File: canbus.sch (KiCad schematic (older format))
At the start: 15 parts, among them J1 Conn_01x08, J2 RJ45, J3 RJ45, U1 MCP2515-E/SO, U2 MCP2562-H/SN, Y1 Crystal_GND24

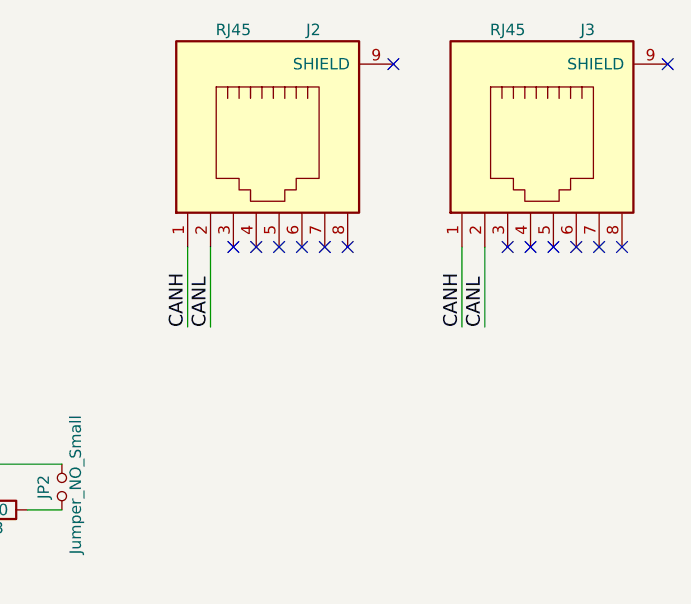
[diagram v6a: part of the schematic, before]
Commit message: Added gnd to RJ45 and connected all pins for passthrough
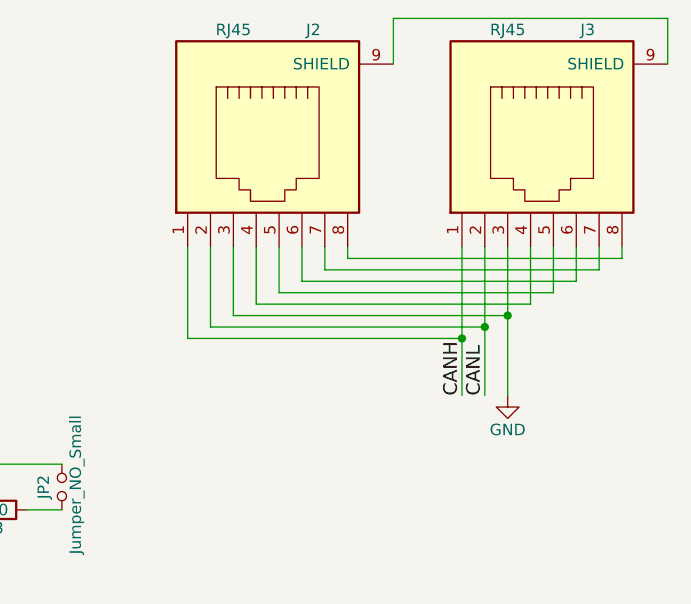
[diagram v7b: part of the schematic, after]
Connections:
- net GND: now also J2.3, J3.3
- net at J2.4: now also J3.4
- net at J2.5: now also J3.5
- net at J2.6: now also J3.6
- net at J2.7: now also J3.7
- net at J2.8: now also J3.8
- net at J2.9 (SHIELD): now also J3.9 (SHIELD)
- no-connect marks 20 -> 6
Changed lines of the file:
@@
 	1    0    0    -1
 $EndComp
-$Comp
-L RJ45 J2
-U 1 1 59E43703
-P 8550 1500
-F 0 "J2" H 8750 2000 50  0000 C CNN
-F 1 "RJ45" H 8400 2000 50  0000 C CNN
-F 2 "Connectors:RJ45_8" H 8550 1500 50  0001 C CNN
-F 3 "" H 8550 1500 50  0001 C CNN
-	1    8550 1500
-	1    0    0    -1
-$EndComp
-$Comp
-L RJ45 J3
-U 1 1 59E43803
-P 9750 1500
-F 0 "J3" H 9950 2000 50  0000 C CNN
-F 1 "RJ45" H 9600 2000 50  0000 C CNN
-F 2 "Connectors:RJ45_8" H 9750 1500 50  0001 C CNN
-F 3 "" H 9750 1500 50  0001 C CNN
-	1    9750 1500
-	1    0    0    -1
-$EndComp
-NoConn ~ 10300 1150
-NoConn ~ 9100 1150
 Text Label 6900 3100 0    60   ~ 0
 CANL
@@
 	1    0    0    -1
 $EndComp
-Text Label 8200 2300 1    60   ~ 0
+Text Label 9400 2600 1    60   ~ 0
 CANH
-Text Label 8300 2300 1    60   ~ 0
-CANL
-Text Label 9400 2300 1    60   ~ 0
-CANH
-Text Label 9500 2300 1    60   ~ 0
+Text Label 9500 2600 1    60   ~ 0
 CANL
 $Comp
@@
 	1    0    0    -1
 $EndComp
-Wire Wire Line
-	5050 2650 5500 2650
-Wire Wire Line
-	5500 2650 5500 2800
-Wire Wire Line
-	5500 2800 5700 2800
-Wire Wire Line
-	5050 2550 5400 2550
-Wire Wire Line
-	5400 2550 5400 2900
-Wire Wire Line
-	5400 2900 5700 2900
-Wire Wire Line
-	6700 3100 7200 3100
-Wire Wire Line
-	7500 3100 7650 3100
-Wire Wire Line
-	6700 2900 7650 2900
-Wire Wire Line
-	5700 3200 5600 3200
-Wire Wire Line
-	5600 3200 5600 3300
-Wire Wire Line
-	5600 3600 5600 3700
-Wire Wire Line
-	6200 3700 6200 3400
-Wire Wire Line
-	5450 3100 5700 3100
-Wire Wire Line
-	4450 4250 4450 3950
-Wire Wire Line
-	4450 2050 4450 2350
-Wire Wire Line
-	6200 2300 6200 2600
-Wire Wire Line
-	8200 2300 8200 1950
-Wire Wire Line
-	8300 2300 8300 1950
-Wire Wire Line
-	9400 2300 9400 1950
-Wire Wire Line
-	9500 2300 9500 1950
-Wire Wire Line
-	3600 3600 3600 3450
-Wire Wire Line
-	3600 3450 3850 3450
-Wire Wire Line
-	3300 3600 3300 3350
-Wire Wire Line
-	3300 3350 3850 3350
-Wire Wire Line
-	3450 3800 3450 4050
-Wire Wire Line
-	5050 3750 5150 3750
-Wire Wire Line
-	5150 3750 5150 3850
-Wire Wire Line
-	5150 4450 5150 4150
-Wire Wire Line
-	5050 3150 5350 3150
-Wire Wire Line
-	3550 2850 3850 2850
-Wire Wire Line
-	3850 2750 3550 2750
-Wire Wire Line
-	3550 2650 3850 2650
-Wire Wire Line
-	3850 2550 3550 2550
-Wire Wire Line
-	2350 5200 2350 5300
-Wire Wire Line
-	2350 5300 2450 5300
-Wire Wire Line
-	2950 5300 3050 5300
-Wire Wire Line
-	3050 5300 3050 5200
-Wire Wire Line
-	1900 2250 1900 2350
-Wire Wire Line
-	1900 2350 2000 2350
-Wire Wire Line
-	1800 2550 2000 2550
-Wire Wire Line
-	1800 2650 2000 2650
-Wire Wire Line
-	1800 2750 2000 2750
-Wire Wire Line
-	1800 2850 2000 2850
-Wire Wire Line
-	1800 2950 2000 2950
-Wire Wire Line
-	1900 3150 1900 3050
-Wire Wire Line
-	1900 3050 2000 3050
-Wire Wire Line
-	1700 2350 1700 2450
-Wire Wire Line
-	1700 2450 2000 2450
-Wire Wire Line
-	2700 5400 2700 5650
-Wire Wire Line
-	4200 5350 4550 5350
-Wire Wire Line
-	4200 5350 4200 5250
-Connection ~ 4300 5350
-Wire Wire Line
-	3650 5350 4000 5350
-Wire Wire Line
-	3650 5350 3650 5250
-Connection ~ 3750 5350
-Wire Wire Line
-	3650 5750 3650 5650
-Wire Wire Line
-	3650 5650 4000 5650
-Connection ~ 3750 5650
-Wire Wire Line
-	4200 5750 4200 5650
-Wire Wire Line
-	4200 5650 4550 5650
-Connection ~ 4300 5650
-Wire Wire Line
-	3450 3400 3450 3250
-Wire Wire Line
-	3450 3250 3200 3250
-Wire Wire Line
-	3200 3250 3200 3900
-Wire Wire Line
-	3200 3900 3450 3900
-Connection ~ 3450 3900
-NoConn ~ 8400 1950
-NoConn ~ 8500 1950
-NoConn ~ 8600 1950
-NoConn ~ 8700 1950
-NoConn ~ 8800 1950
-NoConn ~ 8900 1950
-NoConn ~ 9600 1950
-NoConn ~ 9700 1950
-NoConn ~ 9800 1950
-NoConn ~ 9900 1950
-NoConn ~ 10000 1950
-NoConn ~ 10100 1950
 $Comp
 L MCP2515-E/SO U1
@@
 	1    0    0    -1
 $EndComp
+$Comp
+L RJ45 J2
+U 1 1 59E43703
+P 8550 1500
+F 0 "J2" H 8750 2000 50  0000 C CNN
+F 1 "RJ45" H 8400 2000 50  0000 C CNN
+F 2 "Connectors:RJ45_8" H 8550 1500 50  0001 C CNN
+F 3 "" H 8550 1500 50  0001 C CNN
+	1    8550 1500
+	1    0    0    -1
+$EndComp
+$Comp
+L RJ45 J3
+U 1 1 59E43803
+P 9750 1500
+F 0 "J3" H 9950 2000 50  0000 C CNN
+F 1 "RJ45" H 9600 2000 50  0000 C CNN
+F 2 "Connectors:RJ45_8" H 9750 1500 50  0001 C CNN
+F 3 "" H 9750 1500 50  0001 C CNN
+	1    9750 1500
+	1    0    0    -1
+$EndComp
+Wire Wire Line
+	5050 2650 5500 2650
+Wire Wire Line
+	5500 2650 5500 2800
+Wire Wire Line
+	5500 2800 5700 2800
+Wire Wire Line
+	5050 2550 5400 2550
+Wire Wire Line
+	5400 2550 5400 2900
+Wire Wire Line
+	5400 2900 5700 2900
+Wire Wire Line
+	6700 3100 7200 3100
+Wire Wire Line
+	7500 3100 7650 3100
+Wire Wire Line
+	6700 2900 7650 2900
+Wire Wire Line
+	5700 3200 5600 3200
+Wire Wire Line
+	5600 3200 5600 3300
+Wire Wire Line
+	5600 3600 5600 3700
+Wire Wire Line
+	6200 3700 6200 3400
+Wire Wire Line
+	5450 3100 5700 3100
+Wire Wire Line
+	4450 4250 4450 3950
+Wire Wire Line
+	4450 2050 4450 2350
+Wire Wire Line
+	6200 2300 6200 2600
+Wire Wire Line
+	3600 3600 3600 3450
+Wire Wire Line
+	3600 3450 3850 3450
+Wire Wire Line
+	3300 3600 3300 3350
+Wire Wire Line
+	3300 3350 3850 3350
+Wire Wire Line
+	3450 3800 3450 4050
+Wire Wire Line
+	5050 3750 5150 3750
+Wire Wire Line
+	5150 3750 5150 3850
+Wire Wire Line
+	5150 4450 5150 4150
+Wire Wire Line
+	5050 3150 5350 3150
+Wire Wire Line
+	3550 2850 3850 2850
+Wire Wire Line
+	3850 2750 3550 2750
+Wire Wire Line
+	3550 2650 3850 2650
+Wire Wire Line
+	3850 2550 3550 2550
+Wire Wire Line
+	2350 5200 2350 5300
+Wire Wire Line
+	2350 5300 2450 5300
+Wire Wire Line
+	2950 5300 3050 5300
+Wire Wire Line
+	3050 5300 3050 5200
+Wire Wire Line
+	1900 2250 1900 2350
+Wire Wire Line
+	1900 2350 2000 2350
+Wire Wire Line
+	1800 2550 2000 2550
+Wire Wire Line
+	1800 2650 2000 2650
+Wire Wire Line
+	1800 2750 2000 2750
+Wire Wire Line
+	1800 2850 2000 2850
+Wire Wire Line
+	1800 2950 2000 2950
+Wire Wire Line
+	1900 3150 1900 3050
+Wire Wire Line
+	1900 3050 2000 3050
+Wire Wire Line
+	1700 2350 1700 2450
+Wire Wire Line
+	1700 2450 2000 2450
+Wire Wire Line
+	2700 5400 2700 5650
+Wire Wire Line
+	4200 5350 4550 5350
+Wire Wire Line
+	4200 5350 4200 5250
+Connection ~ 4300 5350
+Wire Wire Line
+	3650 5350 4000 5350
+Wire Wire Line
+	3650 5350 3650 5250
+Connection ~ 3750 5350
+Wire Wire Line
+	3650 5750 3650 5650
+Wire Wire Line
+	3650 5650 4000 5650
+Connection ~ 3750 5650
+Wire Wire Line
+	4200 5750 4200 5650
+Wire Wire Line
+	4200 5650 4550 5650
+Connection ~ 4300 5650
+Wire Wire Line
+	3450 3400 3450 3250
+Wire Wire Line
+	3450 3250 3200 3250
+Wire Wire Line
+	3200 3250 3200 3900
+Wire Wire Line
+	3200 3900 3450 3900
+Connection ~ 3450 3900
+Wire Wire Line
+	8900 1950 8900 2000
+Wire Wire Line
+	8900 2000 10100 2000
+Wire Wire Line
+	10100 2000 10100 1950
+Wire Wire Line
+	10000 1950 10000 2050
+Wire Wire Line
+	10000 2050 8800 2050
+Wire Wire Line
+	8800 2050 8800 1950
+Wire Wire Line
+	8700 1950 8700 2100
+Wire Wire Line
+	8700 2100 9900 2100
+Wire Wire Line
+	9900 2100 9900 1950
+Wire Wire Line
+	9800 1950 9800 2150
+Wire Wire Line
+	9800 2150 8600 2150
+Wire Wire Line
+	8600 2150 8600 1950
+Wire Wire Line
+	8500 1950 8500 2200
+Wire Wire Line
+	8500 2200 9700 2200
+Wire Wire Line
+	9700 2200 9700 1950
+Wire Wire Line
+	9600 1950 9600 2600
+Wire Wire Line
+	9600 2250 8400 2250
+Wire Wire Line
+	8400 2250 8400 1950
+Wire Wire Line
+	8300 1950 8300 2300
+Wire Wire Line
+	8300 2300 9500 2300
+Wire Wire Line
+	9500 1950 9500 2600
+Wire Wire Line
+	9400 1950 9400 2600
+Wire Wire Line
+	9400 2350 8200 2350
+Wire Wire Line
+	8200 2350 8200 1950
+Connection ~ 9400 2350
+Connection ~ 9500 2300
+Wire Wire Line
+	9100 1150 9100 950
+Wire Wire Line
+	9100 950  10300 950
+Wire Wire Line
+	10300 950  10300 1150
+Connection ~ 9600 2250
+$Comp
+L GND #PWR?
+U 1 1 59FCC298
+P 9600 2600
+F 0 "#PWR?" H 9600 2350 50  0001 C CNN
+F 1 "GND" H 9600 2450 50  0000 C CNN
+F 2 "" H 9600 2600 50  0001 C CNN
+F 3 "" H 9600 2600 50  0001 C CNN
+	1    9600 2600
+	1    0    0    -1
+$EndComp

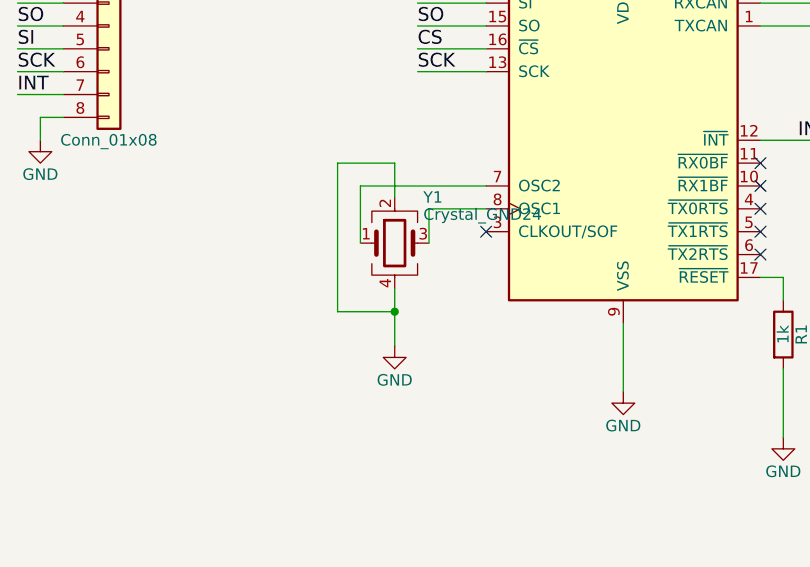
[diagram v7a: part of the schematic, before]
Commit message: Added missing capacitors for oscillator
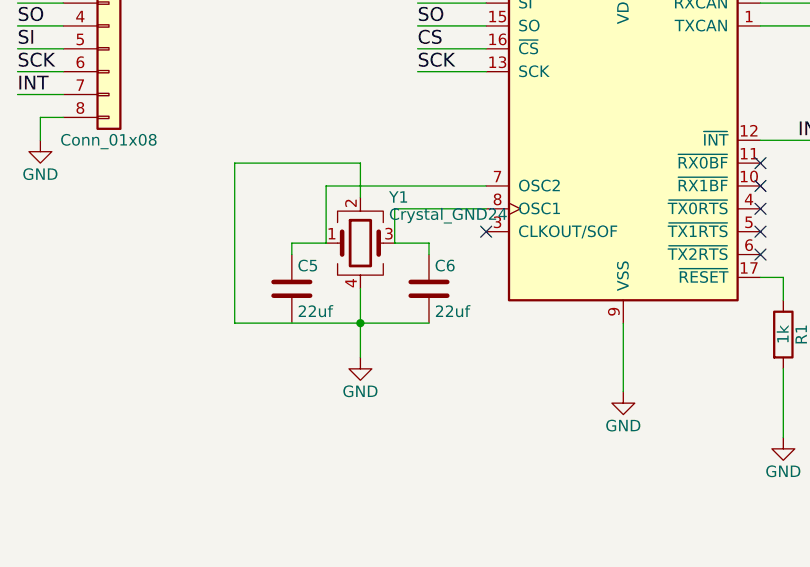
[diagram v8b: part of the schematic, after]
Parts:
- added C5, C6: 22uf, Capacitors_SMD:C_0805_HandSoldering, symbol C
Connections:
- net GND: now also C6.2
- net at U1.7 (OSC2), Y1.1: now also C5.1
- net at U1.8 (OSC1), Y1.3: now also C6.1
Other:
- moved on the sheet: Y1
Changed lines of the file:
@@
 LIBS:valves
 LIBS:MCP2515-E.SO
+LIBS:Accessories
+LIBS:Addressable_Specialty
+LIBS:Alarms_Buzzers_and_Sirens
+LIBS:Balun
+LIBS:Barrel-Audio_Connectors
+LIBS:Capacitive_Touch_Sensors_Proximity_Sensor_ICs
+LIBS:Clock-Timing-Clock_Generators_PLLs_Frequency_Synthesizers
+LIBS:Clock-Timing-Programmable_Timers_and_Oscillators
+LIBS:Clock-Timing-Real_Time_Clocks
+LIBS:Coaxial_Connectors_(RF)
+LIBS:Current_Transducers
+LIBS:Data_Acquisition-ADCs-DACs-Special_Purpose
+LIBS:Data_Acquisition-Analog_to_Digital_Converters_(ADC)
+LIBS:Data_Acquisition-Digital_Potentiometers
+LIBS:Data_Acquisition-Digital_to_Analog_Converters_(DAC)
+LIBS:Data_Acquisition-Touch_Screen_Controllers
+LIBS:DC_DC_Converters
+LIBS:Digital_Isolators
+LIBS:Diodes-Bridge_Rectifiers
+LIBS:Diodes-Rectifiers-Arrays
+LIBS:Diodes-Rectifiers-Single
+LIBS:Diodes-Zener-Single
+LIBS:Display_Modules-LED_Character_and_Numeric
+LIBS:D-Sub_Connectors
+LIBS:Embedded-Microcontrollers
+LIBS:Encoders
+LIBS:Evaluation_Boards-Embedded-MCU_DSP
+LIBS:Evaluation_Boards-Sensors
+LIBS:Ferrite_Beads_and_Chips
+LIBS:Fixed_Inductors
+LIBS:Fuses
+LIBS:Gas_Sensors
+LIBS:Humidity_Moisture_Sensors
+LIBS:Image_Sensors_Camera
+LIBS:Infrared_UV_Visible_Emitters
+LIBS:Inrush_Current_Limiters_(ICL)
+LIBS:Interface-Analog_Switches_Multiplexers_Demultiplexers
+LIBS:Interface-Analog_Switches-Special_Purpose
+LIBS:Interface-Controllers
+LIBS:Interface-Drivers_Receivers_Transceivers
+LIBS:Interface-I-O_Expanders
+LIBS:Interface-Modules
+LIBS:Interface-Sensor_and_Detector_Interfaces
+LIBS:Interface-Specialized
+LIBS:LED_Indication-Discrete
+LIBS:LEDs-Circuit_Board_Indicators_Arrays_Light_Bars_Bar_Graphs
+LIBS:Linear-Amplifiers-Audio
+LIBS:Linear-Amplifiers-Instrumentation_OP_Amps_Buffer_Amps
+LIBS:Linear-Comparators
+LIBS:Logic-Buffers_Drivers_Receivers_Transceivers
+LIBS:Logic-Flip_Flops
+LIBS:Logic-Gates_and_Inverters
+LIBS:Logic-Multivibrators
+LIBS:Logic-Shift_Registers
+LIBS:Logic-Signal_Switches_Multiplexers_Decoders
+LIBS:Logic-Translators_Level_Shifters
+LIBS:Magnetic_Sensors-Compass_Magnetic_Field_(Modules)
+LIBS:Magnetic_Sensors-Linear_Compass_(ICs)
+LIBS:Magnetic_Sensors-Switches_(Solid_State)
+LIBS:Memory_Connectors-PC_Card_Sockets
+LIBS:Microphones
+LIBS:Modular_Connectors-Jacks
+LIBS:Modular_Connectors-Jacks_With_Magnetics
+LIBS:Motion_Sensors-Accelerometers
+LIBS:Motion_Sensors-IMUs_(Inertial_Measurement_Units)
+LIBS:Motion_Sensors-Tilt_Switches
+LIBS:Navigation_Switches_Joystick
+LIBS:Optical_Sensors-Ambient_Light_IR_UV_Sensors
+LIBS:Optical_Sensors-Photo_Detectors-Remote_Receiver
+LIBS:Optical_Sensors-Photodiodes
+LIBS:Optical_Sensors-Photointerrupters-Slot_Type-Logic_Output
+LIBS:Optical_Sensors-Phototransistors
+LIBS:Optical_Sensors-Reflective-Analog_Output
+LIBS:Optoisolators-Logic_Output
+LIBS:Optoisolators-Transistor_Photovoltaic_Output
+LIBS:Optoisolators-Triac_SCR_Output
+LIBS:Oscillators
+LIBS:PMIC-AC_DC_Converters_Offline_Switchers
+LIBS:PMIC-Battery_Chargers
+LIBS:PMIC-Battery_Management
+LIBS:PMIC-Current_Regulation-Management
+LIBS:PMIC-Full_Half-Bridge_Drivers
+LIBS:PMIC-Gate_Drivers
+LIBS:PMIC-LED_Drivers
+LIBS:PMIC-Motor_Drivers_Controllers
+LIBS:PMIC-OR_Controllers_Ideal_Diodes
+LIBS:PMIC-Power_Distribution_Switches_Load_Drivers
+LIBS:PMIC-Power_Management-Specialized
+LIBS:PMIC-RMS_to_DC_Converters
+LIBS:PMIC-Supervisors
+LIBS:PMIC-Thermal_Management
+LIBS:PMIC-V-F_and_F-V_Converters
+LIBS:PMIC-Voltage_Reference
+LIBS:PMIC-Voltage_Regulators-DC_DC_Switching_Controllers
+LIBS:PMIC-Voltage_Regulators-DC_DC_Switching_Regulators
+LIBS:PMIC-Voltage_Regulators-Linear
+LIBS:PMIC-Voltage_Regulators-Special_Purpose
+LIBS:Power_Relays_Over_2_Amps
+LIBS:Pressure_Sensors_Transducers
+LIBS:Programmable_Oscillators
+LIBS:Pushbutton_Switches
+LIBS:Rectangular_Connectors-Headers_Male_Pins
+LIBS:Resistor_Networks_Arrays
+LIBS:RF_Amplifiers
+LIBS:RF_Antennas
+LIBS:RF_Demodulators
+LIBS:RF_Detectors
+LIBS:RF_Evaluation_and_Development_Kits_Boards
+LIBS:RF_Receivers
+LIBS:RF_Switches
+LIBS:RF_Transceiver_ICs
+LIBS:RF_Transceiver_Modules
+LIBS:RF_Transmitters
+LIBS:RFID_RF_Access_Monitoring_ICs
+LIBS:Rotary_Potentiometers_Rheostats
+LIBS:Signal_Relays_Up_to_2_Amps
+LIBS:Slide_Switches
+LIBS:Sockets_for_ICs_Transistors
+LIBS:Solid_State_Relays
+LIBS:Specialized_ICs
+LIBS:Specialized_Sensors
+LIBS:Surge_Suppression_ICs
+LIBS:Tactile_Switches
+LIBS:Temperature_Sensors-Analog_and_Digital_Output
+LIBS:Thermal_Cutoffs_(Thermal_Fuses)
+LIBS:Thyristors-DIACs_SIDACs
+LIBS:Thyristors-SCRs
+LIBS:Thyristors-TRIACs
+LIBS:Toggle_Switches
+LIBS:Transistors-Bipolar_(BJT)-Arrays
+LIBS:Transistors-Bipolar_(BJT)-RF
+LIBS:Transistors-Bipolar_(BJT)-Single
+LIBS:Transistors-Bipolar_(BJT)-Single_Pre-Biased
+LIBS:Transistors-FETs_MOSFETs-Arrays
+LIBS:Transistors-FETs_MOSFETs-RF
+LIBS:Transistors-FETs_MOSFETs-Single
+LIBS:Transistors-JFETs
+LIBS:Trimmer_Potentiometers
+LIBS:TVS-Diodes
+LIBS:TVS-Mixed_Technology
+LIBS:USB_DVI_HDMI_Connectors
 LIBS:canbus-cache
 EELAYER 25 0
@@
 L GND #PWR05
 U 1 1 59E47374
-P 3450 4050
-F 0 "#PWR05" H 3450 3800 50  0001 C CNN
-F 1 "GND" H 3450 3900 50  0000 C CNN
-F 2 "" H 3450 4050 50  0001 C CNN
-F 3 "" H 3450 4050 50  0001 C CNN
-	1    3450 4050
+P 3300 4100
+F 0 "#PWR05" H 3300 3850 50  0001 C CNN
+F 1 "GND" H 3300 3950 50  0000 C CNN
+F 2 "" H 3300 4100 50  0001 C CNN
+F 3 "" H 3300 4100 50  0001 C CNN
+	1    3300 4100
 	1    0    0    -1
 $EndComp
@@
 L Crystal_GND24 Y1
 U 1 1 59E5B8A2
-P 3450 3600
-F 0 "Y1" H 3575 3800 50  0000 L CNN
-F 1 "Crystal_GND24" H 3575 3725 50  0000 L CNN
-F 2 "Crystals:Crystal_SMD_5032-4pin_5.0x3.2mm" H 3450 3600 50  0001 C CNN
-F 3 "" H 3450 3600 50  0001 C CNN
-	1    3450 3600
+P 3300 3600
+F 0 "Y1" H 3425 3800 50  0000 L CNN
+F 1 "Crystal_GND24" H 3425 3725 50  0000 L CNN
+F 2 "Crystals:Crystal_SMD_5032-4pin_5.0x3.2mm" H 3300 3600 50  0001 C CNN
+F 3 "" H 3300 3600 50  0001 C CNN
+	1    3300 3600
 	1    0    0    -1
 $EndComp
@@
 	6200 2300 6200 2600
 Wire Wire Line
-	3600 3600 3600 3450
-Wire Wire Line
-	3600 3450 3850 3450
-Wire Wire Line
-	3300 3600 3300 3350
-Wire Wire Line
-	3300 3350 3850 3350
-Wire Wire Line
-	3450 3800 3450 4050
+	3450 3600 3450 3450
+Wire Wire Line
+	3450 3450 3850 3450
+Wire Wire Line
+	3150 3600 3150 3350
+Wire Wire Line
+	3150 3350 3850 3350
+Wire Wire Line
+	3300 3800 3300 4100
 Wire Wire Line
 	5050 3750 5150 3750
@@
 Connection ~ 4300 5650
 Wire Wire Line
-	3450 3400 3450 3250
-Wire Wire Line
-	3450 3250 3200 3250
-Wire Wire Line
-	3200 3250 3200 3900
-Wire Wire Line
-	3200 3900 3450 3900
-Connection ~ 3450 3900
+	3300 3400 3300 3250
+Wire Wire Line
+	3300 3250 2750 3250
+Wire Wire Line
+	2750 3250 2750 3950
+Wire Wire Line
+	2750 3950 3600 3950
+Connection ~ 3300 3950
 Wire Wire Line
 	8900 1950 8900 2000
@@
 Connection ~ 9600 2250
 $Comp
-L GND #PWR?
+L GND #PWR016
 U 1 1 59FCC298
 P 9600 2600
-F 0 "#PWR?" H 9600 2350 50  0001 C CNN
+F 0 "#PWR016" H 9600 2350 50  0001 C CNN
 F 1 "GND" H 9600 2450 50  0000 C CNN
 F 2 "" H 9600 2600 50  0001 C CNN
@@
 	1    0    0    -1
 $EndComp
+$Comp
+L C C5
+U 1 1 5B05E18A
+P 3000 3800
+F 0 "C5" H 3025 3900 50  0000 L CNN
+F 1 "22uf" H 3025 3700 50  0000 L CNN
+F 2 "Capacitors_SMD:C_0805_HandSoldering" H 3038 3650 50  0001 C CNN
+F 3 "" H 3000 3800 50  0001 C CNN
+	1    3000 3800
+	1    0    0    -1
+$EndComp
+$Comp
+L C C6
+U 1 1 5B05E20B
+P 3600 3800
+F 0 "C6" H 3625 3900 50  0000 L CNN
+F 1 "22uf" H 3625 3700 50  0000 L CNN
+F 2 "Capacitors_SMD:C_0805_HandSoldering" H 3638 3650 50  0001 C CNN
+F 3 "" H 3600 3800 50  0001 C CNN
+	1    3600 3800
+	1    0    0    -1
+$EndComp
+Wire Wire Line
+	3000 3650 3000 3600
+Wire Wire Line
+	3000 3600 3150 3600
+Wire Wire Line
+	3450 3600 3600 3600
+Wire Wire Line
+	3600 3600 3600 3650
 $EndSCHEMATC
